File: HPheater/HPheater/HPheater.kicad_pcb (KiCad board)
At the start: 2 copper layers, 100 x 100 mm, 2 parts, among them J1 Conn_01x02_Male

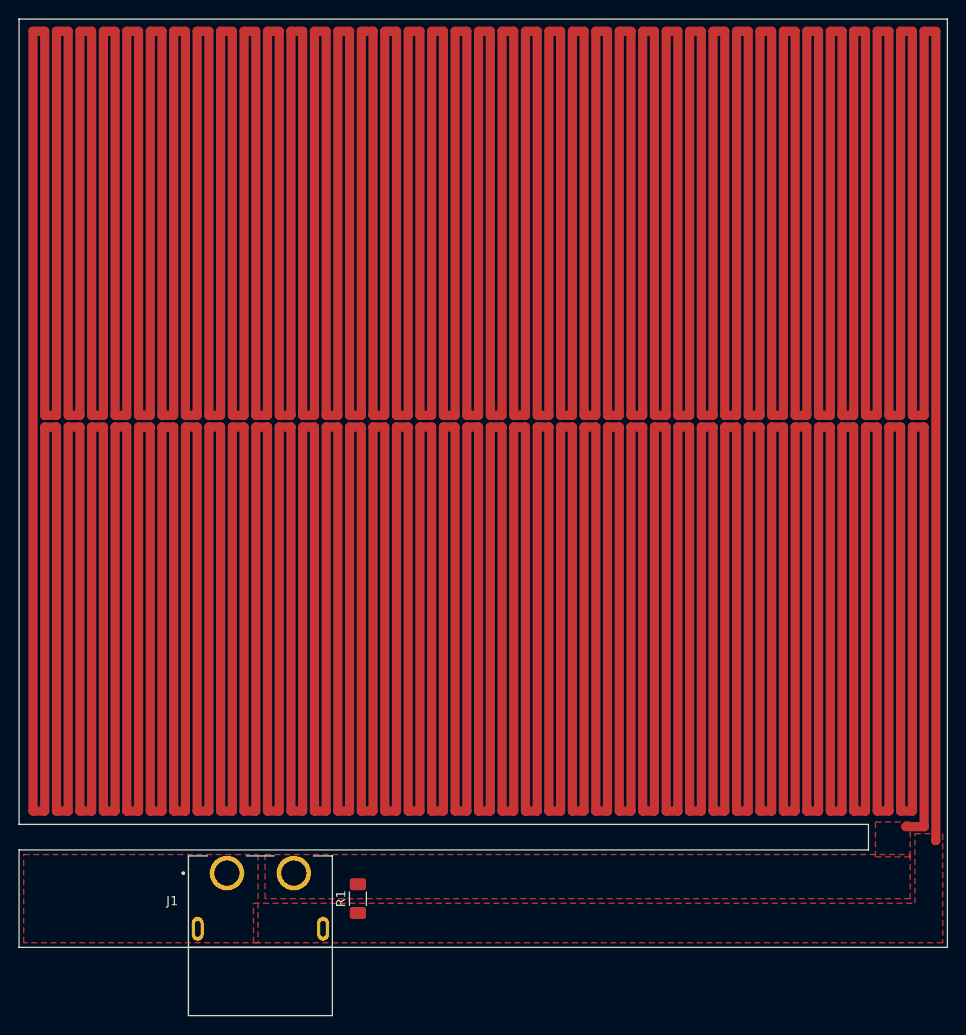
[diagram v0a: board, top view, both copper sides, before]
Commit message: changed heater size, added mounting, refined slot
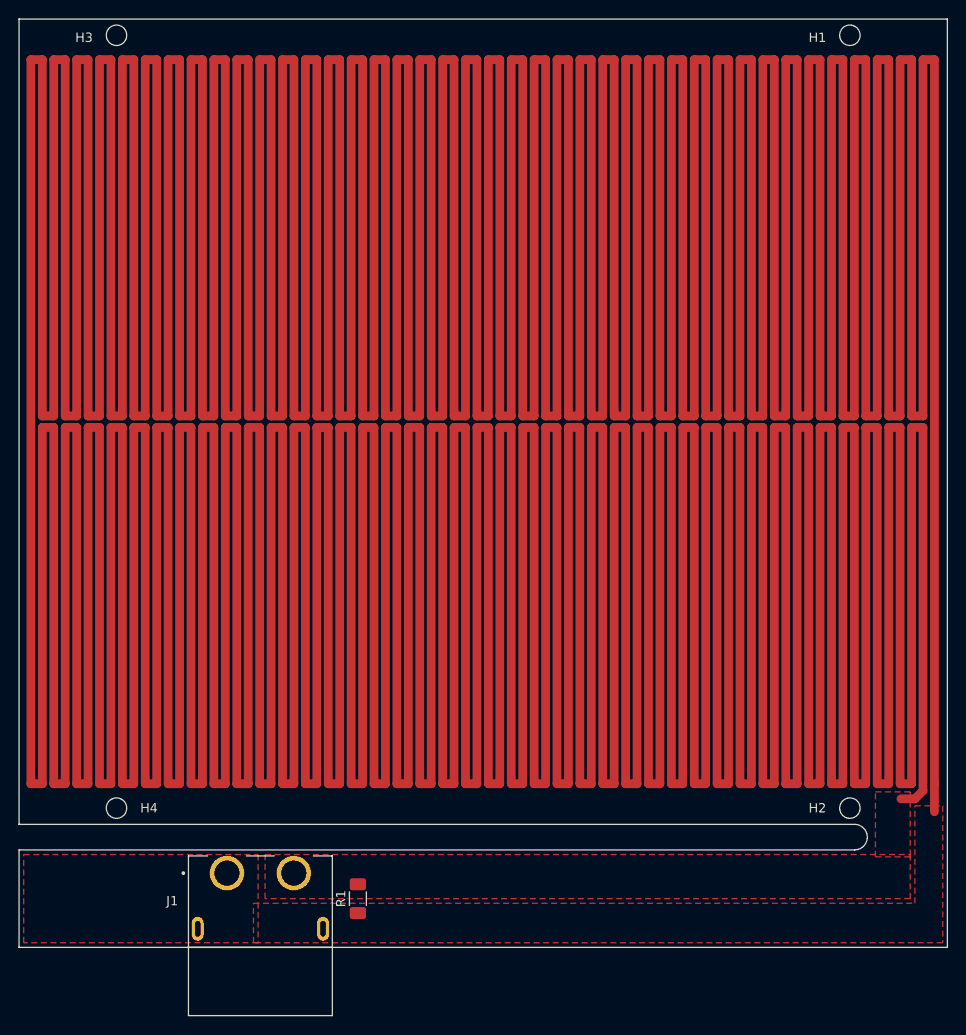
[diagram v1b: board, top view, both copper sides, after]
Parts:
- added H1: MountingHole, MountingHole:MountingHole_2.2mm_M2_ISO14580, F.Cu at (258.5, 20.8)
- added H2: MountingHole, MountingHole:MountingHole_2.2mm_M2_ISO14580, F.Cu at (258.5, 104.0)
- added H3: MountingHole, MountingHole:MountingHole_2.2mm_M2_ISO14580, F.Cu at (179.5, 20.8)
- added H4: MountingHole, MountingHole:MountingHole_2.2mm_M2_ISO14580, F.Cu at (179.5, 104.0)
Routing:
- net (no net): track 6656.1 -> 0.00 mm
- net Net-(J1-Pad1): track 0.00 -> 6343.8 mm
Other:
- outline, holes or cut-outs redrawn
